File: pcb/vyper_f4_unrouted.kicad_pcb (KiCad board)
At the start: 4 copper layers, 36 x 36 mm, 78 parts, among them J1 USB_SERVICE_SH1.0_4P, J2 ESC_SH1.0_8P, J3 RX_UART1, J4 GPS_UART3, J5 AUX_UART4, J6 VTX_UART6, J7 SWD, J8 BEEPER_PAD, U1 STM32F405RGTx, U2 ICM-42688-P, U3 TPS54360DDA, U4 AP2112K-3.3, U5 AP2112K-3.3, U6 W25Q128JVS, U7 BMP280, Y1 8MHz 10pF

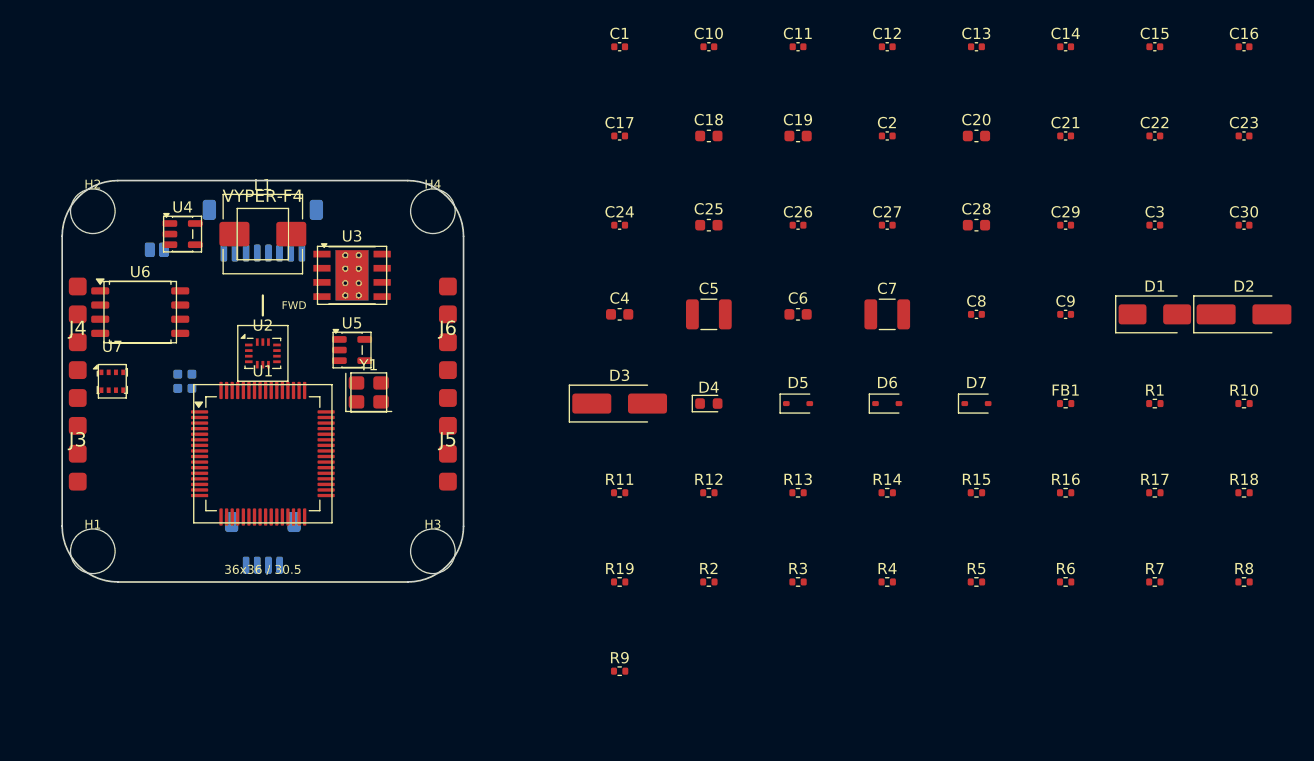
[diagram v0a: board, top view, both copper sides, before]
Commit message: Place all VYPER FC passives in verified 43 mm layout
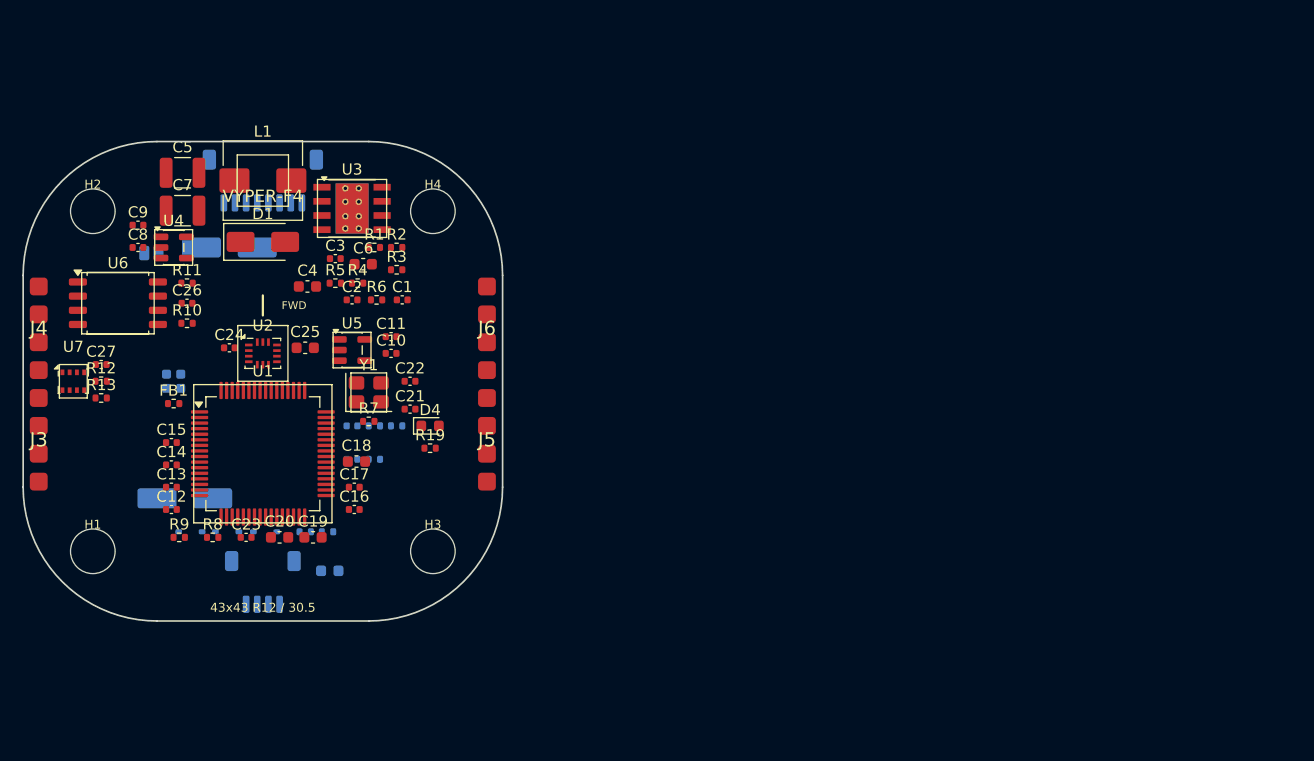
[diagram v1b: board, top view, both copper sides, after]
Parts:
- C28, C29, C30, D2, D3, D5, D6, D7, R14, R15, R16, R17, R18: moved to B.Cu
- moved C23 96.5 mm to (-1.50, 14.0)
- moved C15 95.1 mm to (-8.20, 5.50)
- moved R10 95.1 mm to (-6.80, -5.20)
- moved R8 92.6 mm to (-4.50, 14.0)
- moved D2 91.2 mm to (-3.00, -12.0)
- moved C16 89.9 mm to (8.20, 11.5)
- moved C14 88.5 mm to (-8.20, 7.50)
- moved C9 83.6 mm to (-11.2, -14.0)
- moved C30 82.7 mm to (8.00, 7.00)
- moved C13 82.3 mm to (-8.20, 9.50)
- moved D1 80.3 mm to (0.00, -12.5)
- moved FB1 80.0 mm to (-8.00, 2.00)
- moved R18 78.1 mm to (10.0, 7.00)
- moved C12 76.4 mm to (-8.20, 11.5)
- moved C8 75.4 mm to (-11.2, -12.0)
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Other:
- board size 36 x 36 mm -> 43 x 43 mm
- board text added: "43x43 R12 / 30.5"
- board text removed: "36x36 / 30.5"

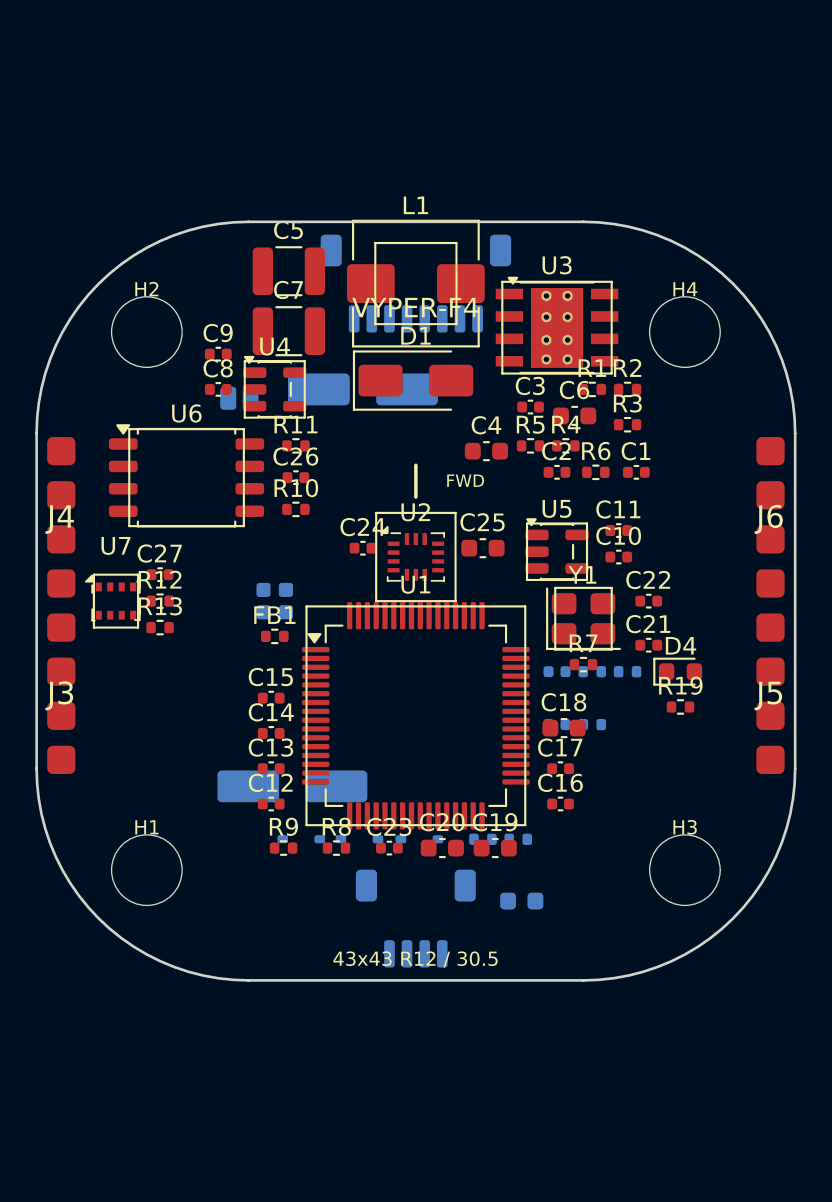
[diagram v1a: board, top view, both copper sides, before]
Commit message: Redesign VYPER around vertical dense electronics
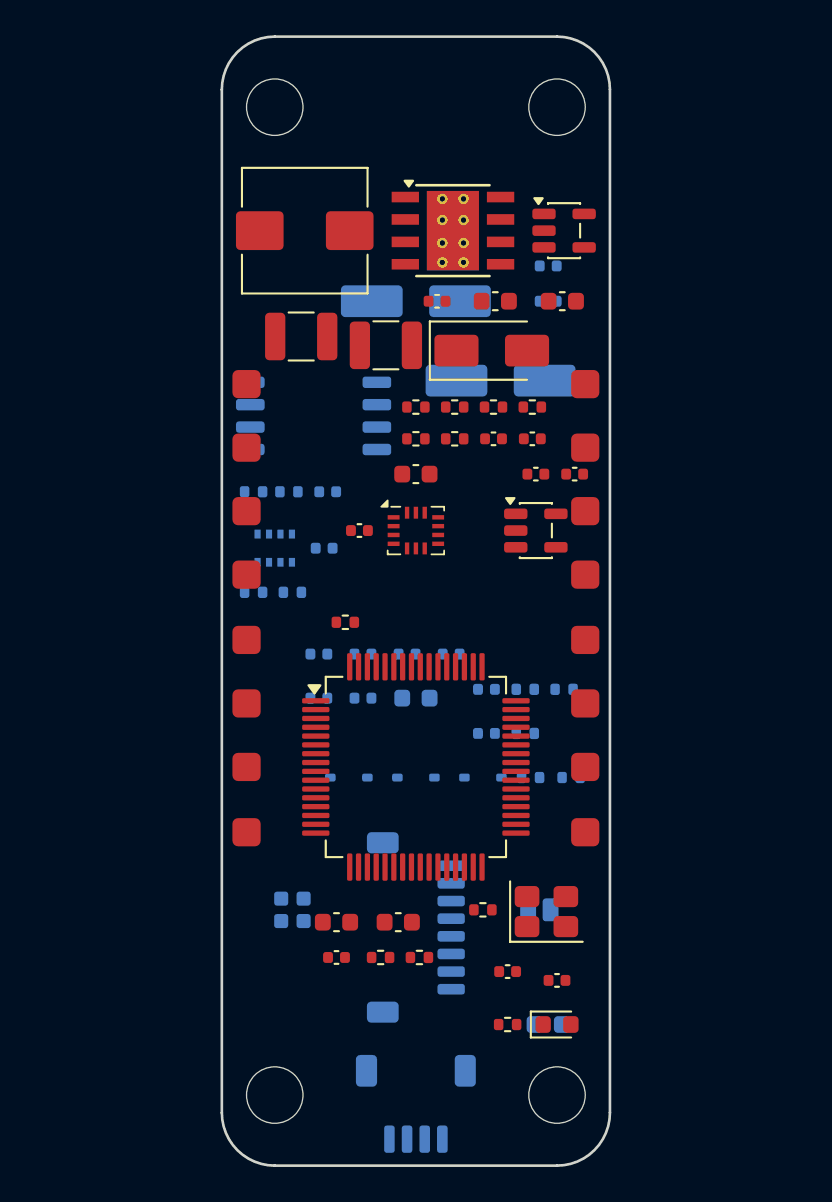
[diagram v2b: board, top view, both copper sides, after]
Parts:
- C12, C13, C14, C15, C16, C17, C18, C26, C27, C8, C9, R10, R11, R12, R13, U6, U7: moved to B.Cu
- moved J2 36.5 mm to (0.00, 18.5), turned to 90 degrees
- moved J8 33.6 mm to (7.00, 17.5)
- moved D3 28.4 mm to (0.00, -17.0)
- moved C22 22.1 mm to (8.00, 21.5)
- moved D4 21.2 mm to (8.00, 24.0)
- moved R19 20.5 mm to (5.20, 24.0)
- moved C21 20.2 mm to (5.20, 21.0)
- moved C8 19.4 mm to (7.50, -17.0)
- moved C9 19.4 mm to (7.50, -19.0)
- moved U4 18.7 mm to (8.40, -21.0)
- moved J7 17.5 mm to (-7.00, 17.5)
- moved Y1 16.7 mm to (7.40, 17.6)
- moved R7 15.0 mm to (3.80, 17.5)
- moved C16 15.0 mm to (-5.50, 5.50)
- moved H1 14.7 mm to (-8.00, 28.0)
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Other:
- board size 43 x 43 mm -> 22 x 64 mm
- board text removed: "43x43 R12 / 30.5"
- board text removed: "FWD"
- board text removed: "VYPER-F4"

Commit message: Add production-size wire pads and reproducible PETG slicing
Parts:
- moved D2 13.0 mm to (-5.00, -21.0)
- moved R11 7.52 mm to (-6.00, -13.0)
- moved U6 5.80 mm to (0.00, -10.5)
- moved R10 4.46 mm to (-6.00, -10.5)
- moved C8 2.69 mm to (10.0, -16.0)
- moved C9 2.50 mm to (10.0, -19.0)
- moved C26 2.06 mm to (-6.00, -8.00)
- moved J3 1.70 mm to (-11.3, 7.65)
- moved J5 1.70 mm to (11.3, 7.65)
- moved J4 1.70 mm to (-11.3, -6.90)
- moved J6 1.70 mm to (11.3, -6.90)
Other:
- board size 22 x 64 mm -> 26 x 64 mm
- board text added: "5V"
- board text added: "ESC"
- board text added: "EVT / UNROUTED"
- board text added: "G"
- board text added: "R1"
- board text added: "R3"
- board text added: "R4"
- board text added: "R6"
- board text added: "T1"
- board text added: "T3"
- board text added: "T4"
- board text added: "T6"
- board text added: "TAIL"
- board text added: "USB"
- board text added: "VYPER-F4 REV A"

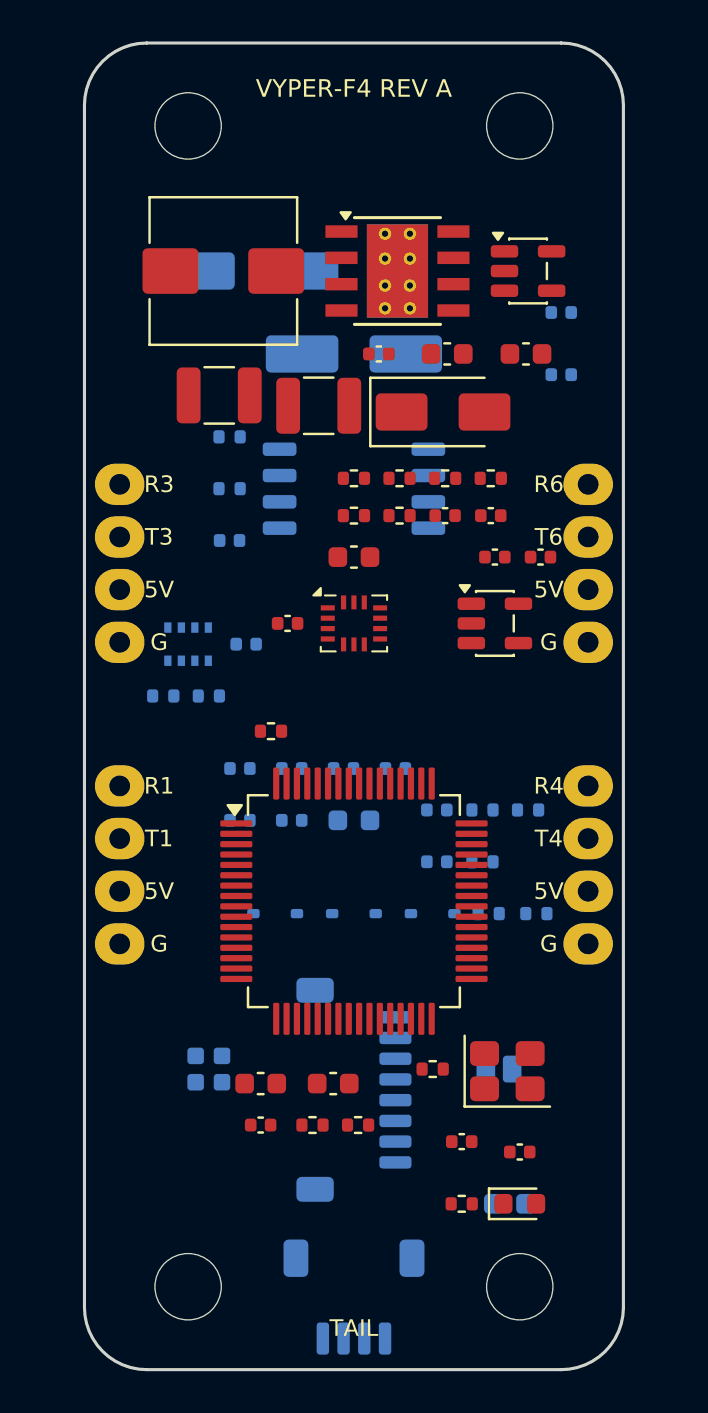
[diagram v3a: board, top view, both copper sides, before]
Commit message: Redesign Vyper FC with sensors and RGB
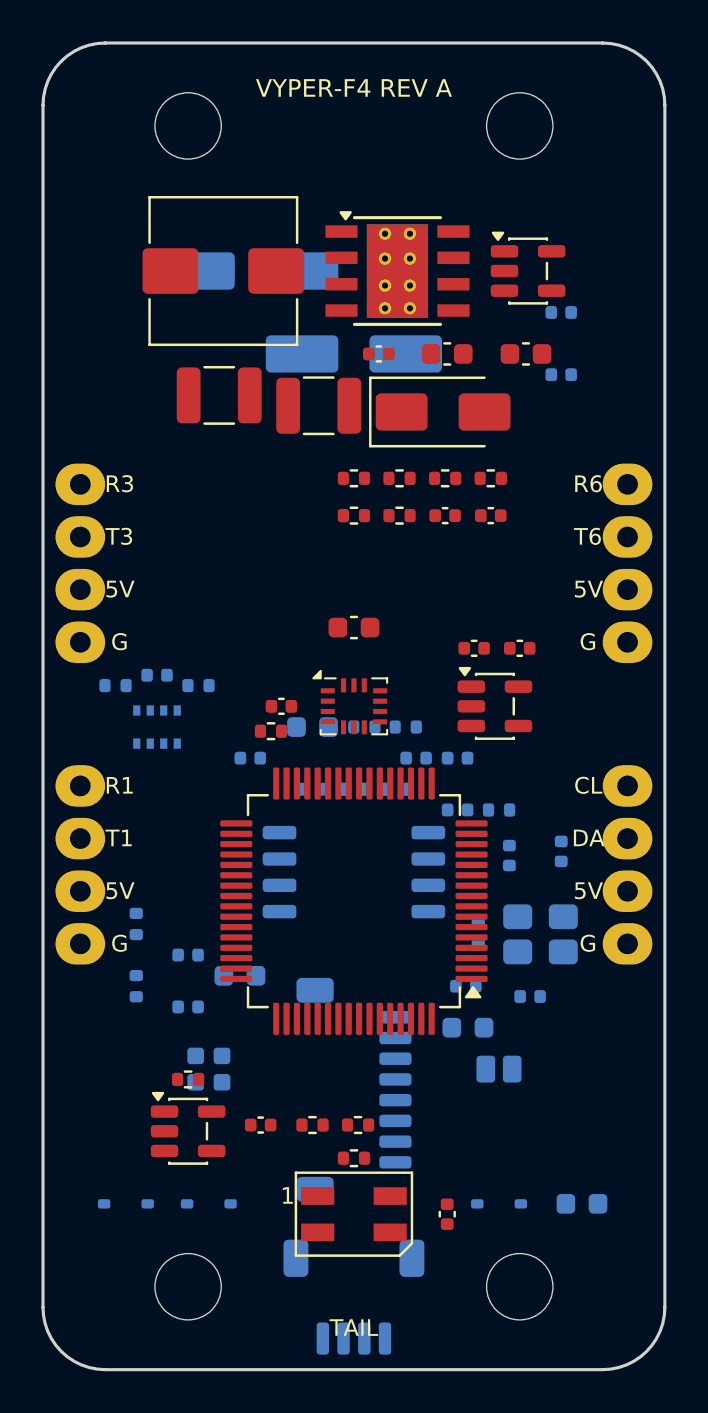
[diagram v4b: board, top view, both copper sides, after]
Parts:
- added C31: 100nF X7R, C_0402_1005Metric, F.Cu at (4.50, 24.5)
- added R20: 100k, R_0402_1005Metric, F.Cu at (-8.00, 18.0)
- added U8: SN74AHCT1G125DBVR, SOT-23-5, F.Cu at (-8.00, 20.5)
- C19, C20, C21, C22, R7, Y1: moved to B.Cu
- D4: value GREEN -> SK6812MINI-E; footprint LED_0603_1608Metric -> LED_SK6812MINI_PLCC4_3.5x3.5mm_P1.75mm
- J5: value AUX_UART4 -> EXTERNAL_I2C
- R19: value 1k -> 33R
- moved R15 19.6 mm to (-10.5, 13.5), turned to 90 degrees
- moved R11 18.8 mm to (2.00, 4.00)
- moved U6 18.5 mm to (0.00, 8.00)
- moved C19 17.4 mm to (-2.00, 1.00)
- moved R14 17.0 mm to (-10.5, 10.5), turned to 90 degrees
- moved D5 15.7 mm to (-11.0, 24.0)
- moved R10 15.7 mm to (0.00, 4.00)
- moved D6 15.7 mm to (-7.00, 24.0)
- moved C22 14.6 mm to (10.0, 7.00), turned to 90 degrees
- moved D7 14.4 mm to (7.00, 24.0)
- moved C21 14.0 mm to (7.50, 7.20), turned to 90 degrees
- moved C14 13.7 mm to (-8.00, 14.5)
- moved C16 13.5 mm to (5.40, 13.5)
- moved C15 12.8 mm to (8.50, 14.0)
- moved C26 12.6 mm to (-2.00, 4.00)
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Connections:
- D4 pad 1: LED_STATUS -> (no net)
- D4 pad 2: N$1 -> GND
- J5 pad 3: AUX_UART4_TX -> I2C1_SDA
- J5 pad 4: AUX_UART4_RX -> I2C1_SCL
- R19 pad 1: V3V3 -> LED_RGB_LEVEL
- R19 pad 2: N$1 -> LED_RGB_DIN
- U1 pad 14: AUX_UART4_TX -> (no net)
- U1 pad 15: AUX_UART4_RX -> (no net)
- U1 pad 41: LED_STATUS -> LED_RGB_MCU
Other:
- board size 26 x 64 mm -> 30 x 64 mm
- board text added: "CL"
- board text added: "DA"
- board text removed: "R4"
- board text removed: "T4"
